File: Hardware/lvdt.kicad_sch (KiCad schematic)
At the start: 27 parts, among them J15 DG250-3-5-06P-11-00AH, U14 MC33204

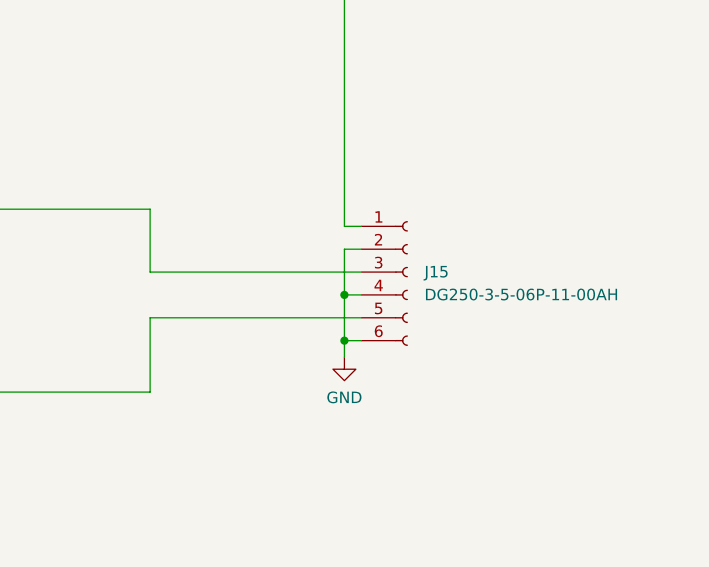
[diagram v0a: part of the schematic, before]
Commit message: Toolchain set. Timer module added. Schematic files migrated.
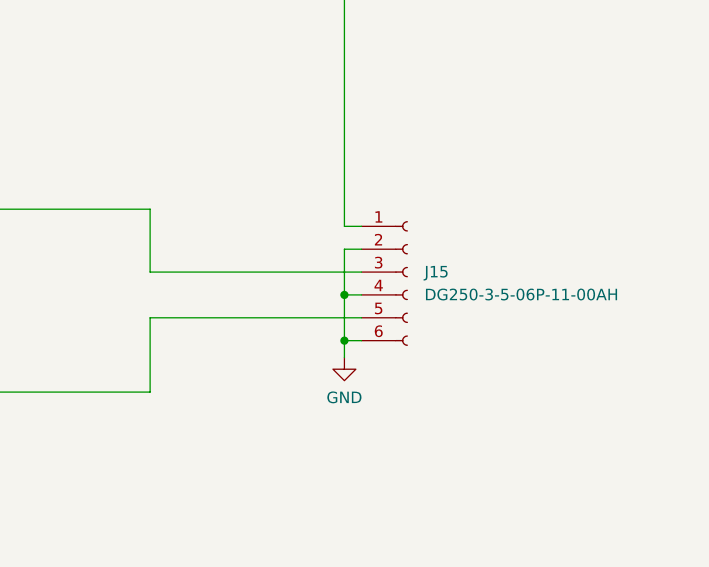
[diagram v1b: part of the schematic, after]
